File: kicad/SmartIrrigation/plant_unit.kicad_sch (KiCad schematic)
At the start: 8 parts

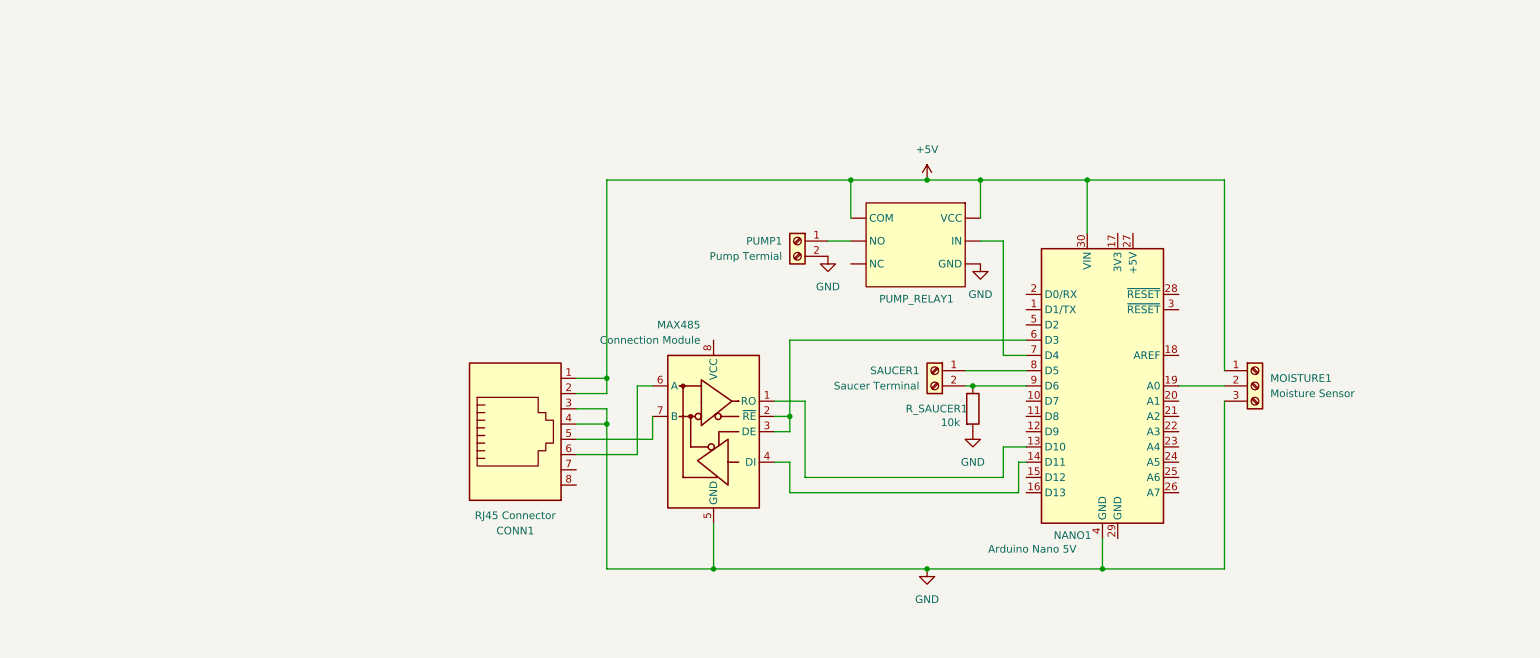
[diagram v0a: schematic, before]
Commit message: Add SDCard class for managing plant data logging and loading
- Created SDCard.cpp and SDCard.h files.
- Implemented methods for loading plant data and logging various plant statuses.
- Prepared the class for future expansion with additional functionalities.
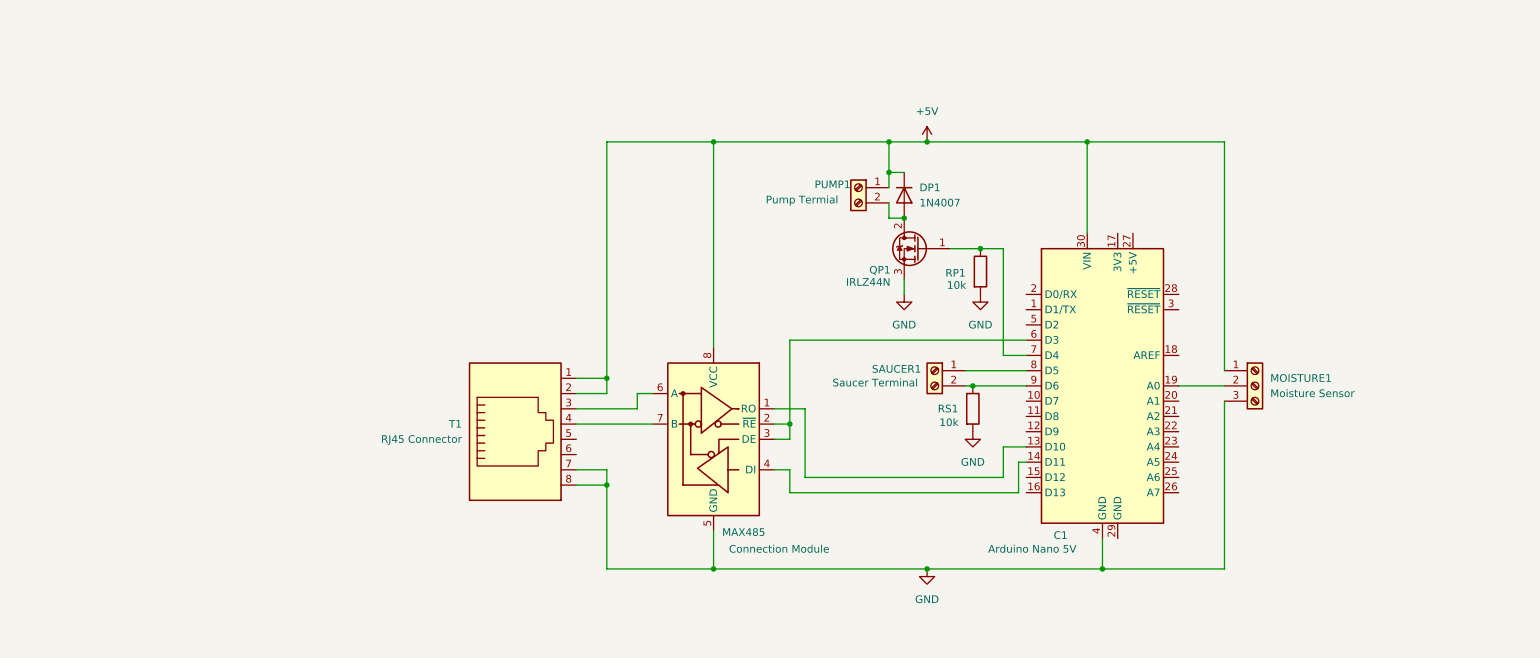
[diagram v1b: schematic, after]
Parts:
- removed PUMP_RELAY1: ~, symbol Relay:Relay
- added DP1: 1N4007, Diode_THT:D_DO-41_SOD81_P10.16mm_Horizontal, symbol Diode:1N4007
- added QP1: IRLZ44N, Package_TO_SOT_THT:TO-220-3_Vertical, symbol Transistor_FET:IRLZ44N
- added RP1: 10k, Resistor_THT:R_Axial_DIN0207_L6.3mm_D2.5mm_P10.16mm_Horizontal, symbol Device:R
- MAX485: footprint (none) -> Package_SO:SOIC-8_3.9x4.9mm_P1.27mm
- MOISTURE1: footprint (none) -> TerminalBlock:TerminalBlock_bornier-3_P5.08mm
- PUMP1, SAUCER1: footprint (none) -> TerminalBlock:TerminalBlock_bornier-2_P5.08mm
- RS1: renamed from R_SAUCER1; footprint (none) -> Resistor_THT:R_Axial_DIN0207_L6.3mm_D2.5mm_P10.16mm_Horizontal
- renumbered NANO1 to C1, CONN1 to T1
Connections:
- net +5V: now also MAX485.8 (VCC), PUMP1.1 (Pin_1), DP1.1 (K)
- net GND: now also T1.7, T1.8, QP1.3 (S), RP1.2; no longer PUMP1.2 (Pin_2), T1.3, T1.4
- net at MAX485.7 (B): now also T1.4; no longer T1.5
- net at MAX485.6 (A): now also T1.3; no longer T1.6
- net at C1.7 (D4): now also QP1.1 (G), RP1.1
- new net: DP1.2 (A), PUMP1.2 (Pin_2), QP1.2 (D)
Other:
- moved on the sheet: MAX485, PUMP1

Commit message: added schematics images
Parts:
- MAX: renamed from MAX485; value Connection Module -> MAX485
- renumbered C1 to NANO, QP1 to NMOS, RP1 to R_MOS, MOISTURE1 to T_MOISTURE, PUMP1 to T_PUMP, SAUCER1 to T_SAUCER
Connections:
- net GND: now also NANO.29 (GND), T1.5, T1.6; no longer NANO.4 (GND)
- net NMOS GATE - NANO D4: now reaches NANO.7 (D4), NMOS.1 (G), R_MOS.1
- net A: now reaches MAX.6 (A), T1.3
- net B: now reaches MAX.7 (B), T1.4
- net MAX RO - NANO D10: now reaches MAX.1 (RO), NANO.13 (D10)
- net MAX DI - NANO D11: now reaches MAX.4 (DI), NANO.14 (D11)
- net T_MOISTURE DATA - NANO A0: now reaches NANO.19 (A0), T_MOISTURE.2 (Pin_2)
- net MAX DE/RE - NANO D3: now reaches MAX.2 (~{RE}), MAX.3 (DE), NANO.6 (D3)
- net at NANO.8 (D5): no longer T_SAUCER.1 (Pin_1)
- net T_SAUCER (-) -  NANO D6: now reaches RS1.1, T_SAUCER.2 (Pin_2)
- net T_SAUCER (-) -  NANO D6: no longer NANO.9 (D6)
- new net T_SAUCER (+) -  NANO D5: T_SAUCER.1 (Pin_1)
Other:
- moved on the sheet: DP1, MAX, NANO, NMOS, RS1, R_MOS, T1, T_MOISTURE, T_PUMP, T_SAUCER
